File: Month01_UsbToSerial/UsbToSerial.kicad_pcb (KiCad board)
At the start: 2 copper layers, 34.9 x 20.3 mm, 14 parts, among them J1 USB_B_Micro, J2 Conn_01x07_Female, J3 Conn_01x07_Female, U1 FT232RL

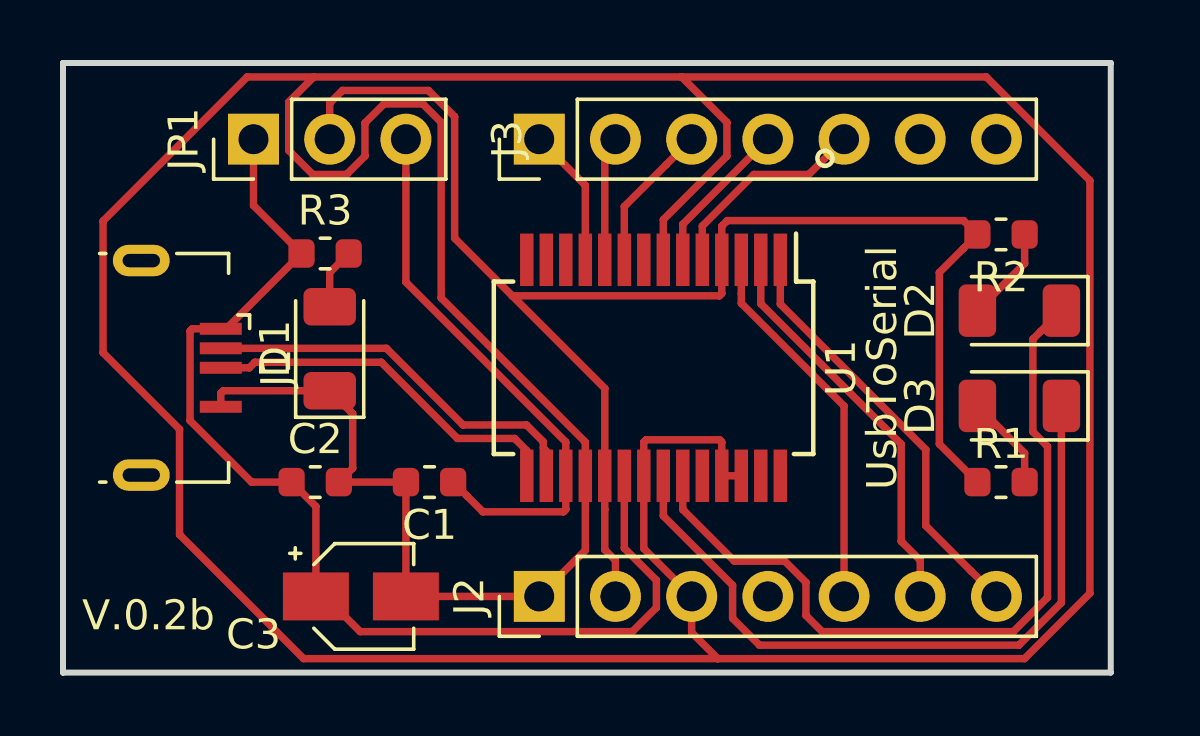
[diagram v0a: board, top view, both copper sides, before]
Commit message: added extra text to the bottom layer of the board, changed pin headers to 8 instead of 7
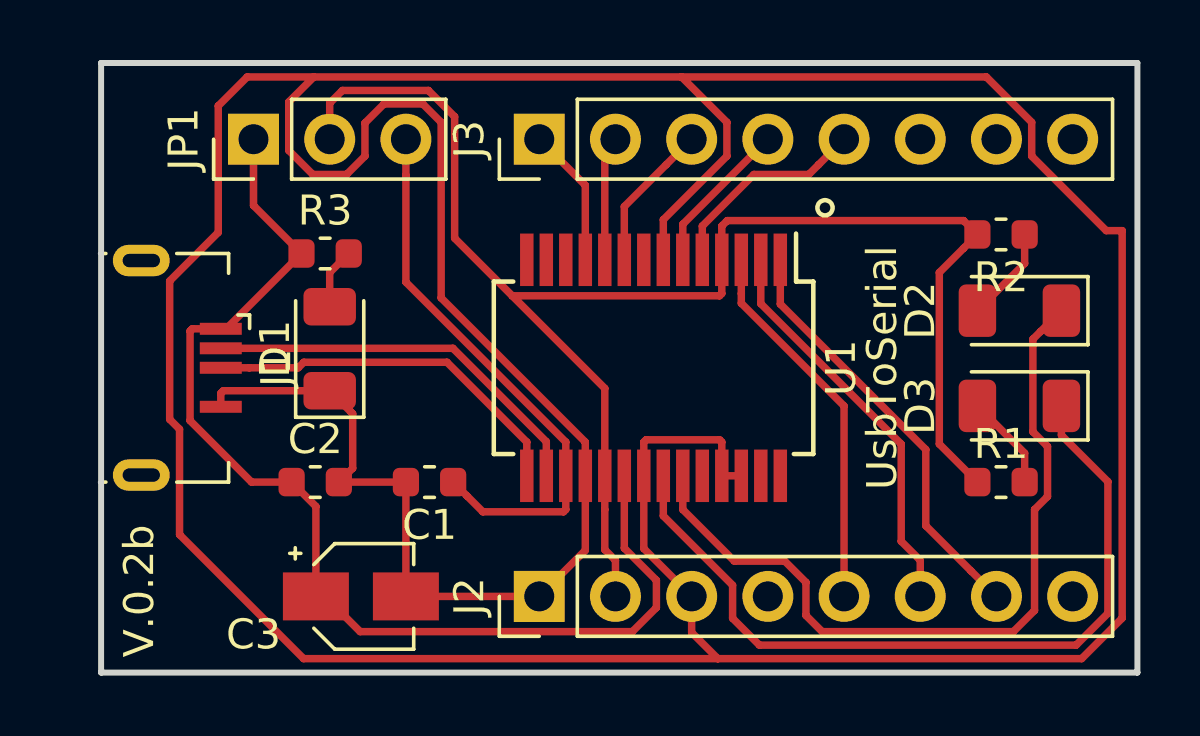
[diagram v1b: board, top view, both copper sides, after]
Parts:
- C3: value (none) -> 10uF
- J2, J3: value Conn_01x07_Female -> Conn_01x08_Male; footprint Connector_PinHeader_2.54mm:PinHeader_1x07_P2.54mm_Vertical -> Connector_PinHeader_2.54mm:PinHeader_1x08_P2.54mm_Vertical
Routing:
- net Net-(D3-Pad1): track 24.2 -> 26.6 mm
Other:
- board size 34.9 x 20.3 mm -> 34.5 x 20.3 mm
- board text added: "CTS"
- board text added: "DCD"
- board text added: "DCR"
- board text added: "DTR"
- board text added: "GND"
- board text added: "PWR"
- board text added: "RI"
- board text added: "RTS"
- board text added: "RXI"
- board text added: "TX0"
